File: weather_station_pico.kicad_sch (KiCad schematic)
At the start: 30 parts, among them J1 POWER, J2 WSPEED, J3 WDIR, J4 I2C, SW1 SW_Push, U1 LM7805_TO220, U2 E220-900T22D, U3 Pico, U4 74HC4051, U5 LM35-LP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

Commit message: ready for plot
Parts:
- gave numbers to parts that had none: 2
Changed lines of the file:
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@@
   (symbol (lib_id "Device:R") (at 148.59 144.78 0) (unit 1)
     (in_bom yes) (on_board yes) (fields_autoplaced)
-    (property "Reference" "R?" (id 0) (at 150.368 143.9453 0)
+    (property "Reference" "R6" (id 0) (at 150.368 143.9453 0)
       (effects (font (size 1.27 1.27)) (justify left))
     )
@@
   (symbol (lib_id "Device:R") (at 156.21 144.78 0) (unit 1)
     (in_bom yes) (on_board yes) (fields_autoplaced)
-    (property "Reference" "R?" (id 0) (at 157.988 143.9453 0)
+    (property "Reference" "R10" (id 0) (at 157.988 143.9453 0)
       (effects (font (size 1.27 1.27)) (justify left))
     )
@@
       (reference "R5") (unit 1) (value "18K") (footprint "Resistor_THT:R_Axial_DIN0207_L6.3mm_D2.5mm_P10.16mm_Horizontal")
     )
+    (path "/951b7f04-3bd9-48e0-a3b1-e47cb09aab6b"
+      (reference "R6") (unit 1) (value "10K") (footprint "Resistor_THT:R_Axial_DIN0207_L6.3mm_D2.5mm_P10.16mm_Horizontal")
+    )
     (path "/15b39b88-b949-4b93-a72b-6f012cecbbf8"
       (reference "R7") (unit 1) (value "10K") (footprint "Resistor_THT:R_Axial_DIN0207_L6.3mm_D2.5mm_P10.16mm_Horizontal")
@@
       (reference "R9") (unit 1) (value "10K") (footprint "Resistor_THT:R_Axial_DIN0207_L6.3mm_D2.5mm_P10.16mm_Horizontal")
     )
-    (path "/951b7f04-3bd9-48e0-a3b1-e47cb09aab6b"
-      (reference "R?") (unit 1) (value "10K") (footprint "Resistor_THT:R_Axial_DIN0207_L6.3mm_D2.5mm_P10.16mm_Horizontal")
-    )
     (path "/da2ad276-2e89-44d0-84db-4f891312c40c"
-      (reference "R?") (unit 1) (value "10K") (footprint "Resistor_THT:R_Axial_DIN0207_L6.3mm_D2.5mm_P10.16mm_Horizontal")
+      (reference "R10") (unit 1) (value "10K") (footprint "Resistor_THT:R_Axial_DIN0207_L6.3mm_D2.5mm_P10.16mm_Horizontal")
     )
     (path "/01ae44e4-73c7-4652-a3e0-80facd31ecc5"

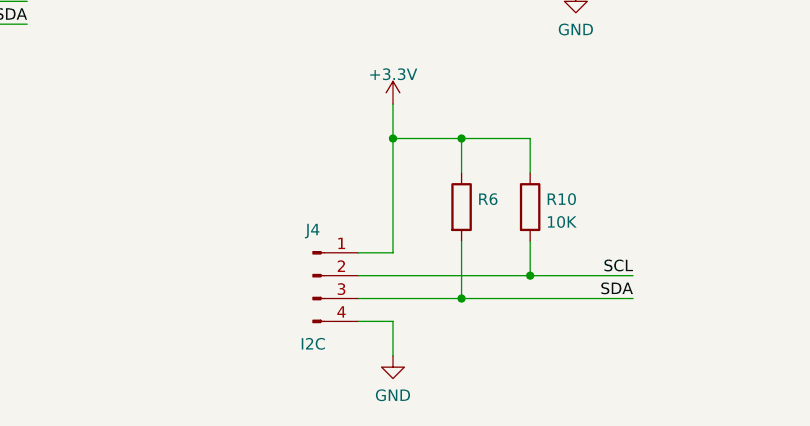
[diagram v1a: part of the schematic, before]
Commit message: add terminal, remove jst connector
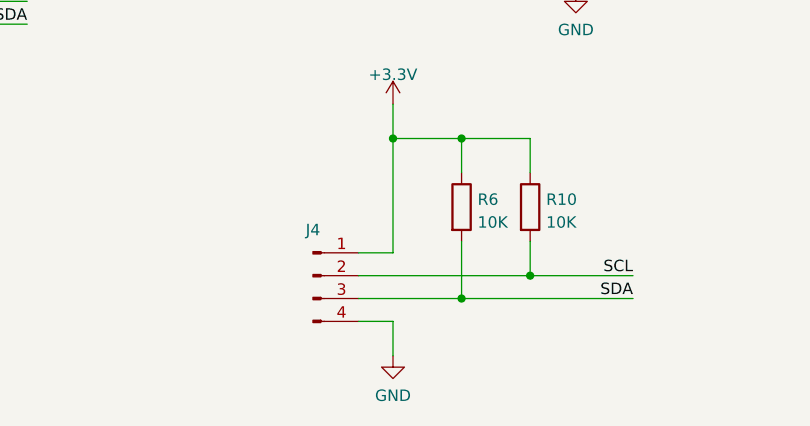
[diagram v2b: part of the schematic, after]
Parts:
- J1: footprint TerminalBlock_TE-Connectivity:TerminalBlock_TE_282834-2_1x02_P2.54mm_Horizontal -> TerminalBlock:TerminalBlock_bornier-2_P5.08mm
- J4: value I2C -> (none); footprint Connector_JST:JST_XH_B4B-XH-A_1x04_P2.50mm_Vertical -> (none)
- R6: value (none) -> 10K
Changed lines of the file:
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@@
     (in_bom yes) (on_board yes)
     (property "Reference" "J4" (id 0) (at 132.08 147.32 0))
-    (property "Value" "I2C" (id 1) (at 132.08 160.02 0))
-    (property "Footprint" "Connector_JST:JST_XH_B4B-XH-A_1x04_P2.50mm_Vertical" (id 2) (at 132.08 152.4 0)
+    (property "Value" "" (id 1) (at 132.08 160.02 0))
+    (property "Footprint" "" (id 2) (at 132.08 152.4 0)
       (effects (font (size 1.27 1.27)) hide)
     )
@@
     (property "Reference" "J1" (id 0) (at 41.91 26.7802 0))
     (property "Value" "POWER" (id 1) (at 41.91 29.3171 0))
-    (property "Footprint" "TerminalBlock_TE-Connectivity:TerminalBlock_TE_282834-2_1x02_P2.54mm_Horizontal" (id 2) (at 41.91 31.75 0)
+    (property "Footprint" "TerminalBlock:TerminalBlock_bornier-2_P5.08mm" (id 2) (at 41.91 31.75 0)
       (effects (font (size 1.27 1.27)) hide)
     )
@@
       (effects (font (size 1.27 1.27)) (justify left))
     )
-    (property "Value" "" (id 1) (at 150.368 146.4822 0)
+    (property "Value" "10K" (id 1) (at 150.368 146.4822 0)
       (effects (font (size 1.27 1.27)) (justify left))
     )
@@
     )
     (path "/950840dd-58ab-430d-9239-f8d51e62b21c"
-      (reference "J1") (unit 1) (value "POWER") (footprint "TerminalBlock_TE-Connectivity:TerminalBlock_TE_282834-2_1x02_P2.54mm_Horizontal")
+      (reference "J1") (unit 1) (value "POWER") (footprint "TerminalBlock:TerminalBlock_bornier-2_P5.08mm")
     )
     (path "/31f5e120-fc67-4891-91d3-9e217a46063f"
@@
     )
     (path "/52d6e53a-c8ef-4b23-a6a7-8729a222959a"
-      (reference "J4") (unit 1) (value "I2C") (footprint "Connector_JST:JST_XH_B4B-XH-A_1x04_P2.50mm_Vertical")
+      (reference "J4") (unit 1) (value "I2C") (footprint "TerminalBlock_TE-Connectivity:TerminalBlock_TE_282834-4_1x04_P2.54mm_Horizontal")
     )
     (path "/26932649-bf50-4889-b6d1-6949f1bf115e"

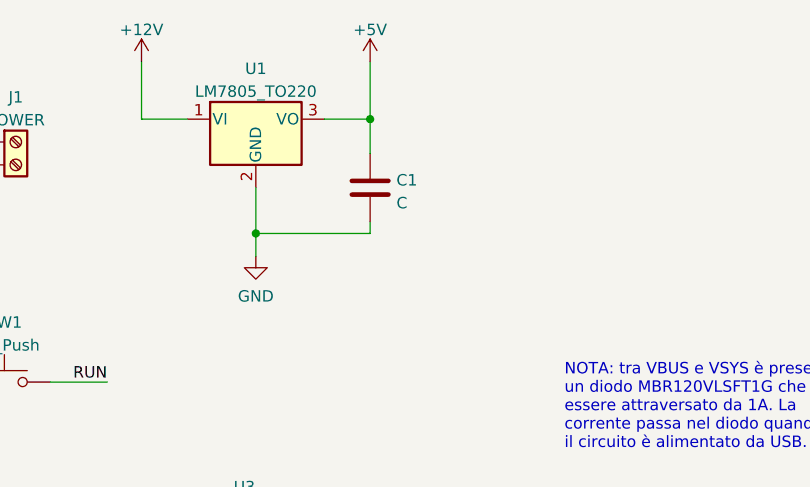
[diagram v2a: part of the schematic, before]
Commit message: move capacitor, more simple track
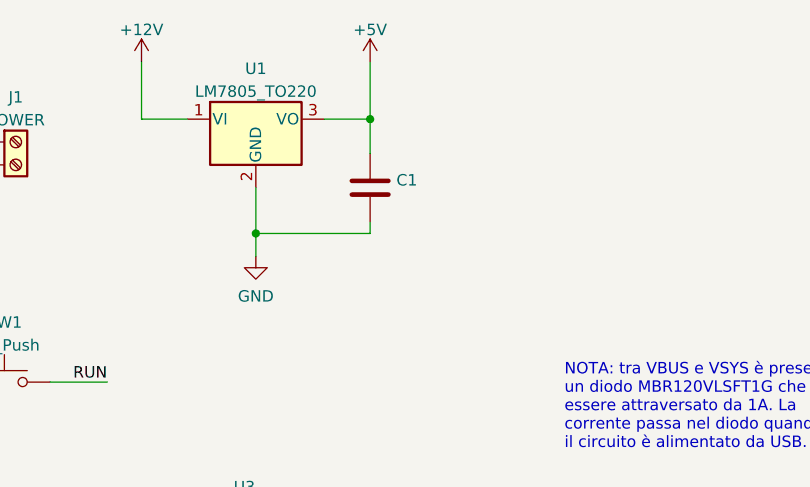
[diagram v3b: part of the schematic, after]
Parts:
- C1: value C -> (none)
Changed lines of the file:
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@@
       (effects (font (size 1.27 1.27)) (justify left))
     )
-    (property "Value" "C" (id 1) (at 84.201 38.5322 0)
+    (property "Value" "" (id 1) (at 84.201 38.5322 0)
       (effects (font (size 1.27 1.27)) (justify left))
     )
@@
     )
     (path "/eb529df0-006e-4c2f-99bd-b038e8ef398f"
-      (reference "C1") (unit 1) (value "C") (footprint "Capacitor_THT:C_Disc_D5.0mm_W2.5mm_P5.00mm")
+      (reference "C1") (unit 1) (value "0.1uF") (footprint "Capacitor_THT:C_Disc_D5.0mm_W2.5mm_P5.00mm")
     )
     (path "/6b3f8bcc-3de8-4f39-8ed0-7c34895de042"

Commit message: add millproject
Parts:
- removed TP1: TEMP_REF, TestPoint:TestPoint_Pad_D1.5mm, symbol Connector:TestPoint
- removed TP2: GND, TestPoint:TestPoint_Pad_D1.5mm, symbol Connector:TestPoint
- removed TP3: TEMP_OUT, TestPoint:TestPoint_Pad_D1.5mm, symbol Connector:TestPoint
- removed TP4: MUX_ADC, TestPoint:TestPoint_Pad_D1.5mm, symbol Connector:TestPoint
- C1: value (none) -> 0.1uF
- J4: value (none) -> I2C; footprint (none) -> TerminalBlock_TE-Connectivity:TerminalBlock_TE_282834-4_1x04_P2.54mm_Horizontal
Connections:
- net GND: no longer U3.42 (GND)
- no-connect marks 21 -> 22
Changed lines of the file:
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@@
   (junction (at 140.97 137.16) (diameter 0) (color 0 0 0 0)
   )
-  (junction (at 146.05 91.44) (diameter 0) (color 0 0 0 0)
-  )
   (junction (at 153.67 26.67) (diameter 0) (color 0 0 0 0)
   )
@@
   (junction (at 34.29 31.75) (diameter 0) (color 0 0 0 0)
   )
-  (junction (at 180.34 99.06) (diameter 0) (color 0 0 0 0)
-  )
   (junction (at 260.35 76.2) (diameter 0) (color 0 0 0 0)
-  )
-  (junction (at 182.88 91.44) (diameter 0) (color 0 0 0 0)
   )
   (junction (at 34.29 34.29) (diameter 0) (color 0 0 0 0)
@@
   (no_connect (at 171.45 104.14))
   (no_connect (at 171.45 101.6))
+  (no_connect (at 67.31 129.54))
   (no_connect (at 49.53 83.82))
   (no_connect (at 49.53 76.2))
@@
     (stroke (width 0) (type default) (color 0 0 0 0))
   )
-  (wire (pts (xy 180.34 99.06) (xy 203.2 99.06))
+  (wire (pts (xy 171.45 99.06) (xy 203.2 99.06))
     (stroke (width 0) (type default) (color 0 0 0 0))
   )
@@
     (stroke (width 0) (type default) (color 0 0 0 0))
   )
-  (wire (pts (xy 146.05 81.28) (xy 146.05 91.44))
-    (stroke (width 0) (type default) (color 0 0 0 0))
-  )
   (wire (pts (xy 68.58 36.83) (xy 68.58 41.91))
     (stroke (width 0) (type default) (color 0 0 0 0))
@@
     (stroke (width 0) (type default) (color 0 0 0 0))
   )
-  (wire (pts (xy 151.13 116.84) (xy 161.29 116.84))
-    (stroke (width 0) (type default) (color 0 0 0 0))
-  )
   (wire (pts (xy 153.67 26.67) (xy 168.91 26.67))
     (stroke (width 0) (type default) (color 0 0 0 0))
@@
     (stroke (width 0) (type default) (color 0 0 0 0))
   )
-  (wire (pts (xy 171.45 99.06) (xy 180.34 99.06))
-    (stroke (width 0) (type default) (color 0 0 0 0))
-  )
   (wire (pts (xy 148.59 137.16) (xy 156.21 137.16))
     (stroke (width 0) (type default) (color 0 0 0 0))
@@
     (stroke (width 0) (type default) (color 0 0 0 0))
   )
-  (wire (pts (xy 146.05 91.44) (xy 153.67 91.44))
-    (stroke (width 0) (type default) (color 0 0 0 0))
-  )
-  (wire (pts (xy 133.35 91.44) (xy 146.05 91.44))
+  (wire (pts (xy 133.35 91.44) (xy 153.67 91.44))
     (stroke (width 0) (type default) (color 0 0 0 0))
   )
@@
     (stroke (width 0) (type default) (color 0 0 0 0))
   )
-  (wire (pts (xy 182.88 91.44) (xy 203.2 91.44))
+  (wire (pts (xy 171.45 91.44) (xy 203.2 91.44))
     (stroke (width 0) (type default) (color 0 0 0 0))
   )
@@
     (stroke (width 0) (type default) (color 0 0 0 0))
   )
-  (wire (pts (xy 180.34 78.74) (xy 180.34 99.06))
-    (stroke (width 0) (type default) (color 0 0 0 0))
-  )
   (wire (pts (xy 260.35 25.4) (xy 260.35 27.94))
     (stroke (width 0) (type default) (color 0 0 0 0))
@@
     (stroke (width 0) (type default) (color 0 0 0 0))
   )
-  (wire (pts (xy 171.45 91.44) (xy 182.88 91.44))
-    (stroke (width 0) (type default) (color 0 0 0 0))
-  )
   (wire (pts (xy 137.16 157.48) (xy 140.97 157.48))
     (stroke (width 0) (type default) (color 0 0 0 0))
@@
     (stroke (width 0) (type default) (color 0 0 0 0))
   )
-  (wire (pts (xy 182.88 83.82) (xy 182.88 91.44))
-    (stroke (width 0) (type default) (color 0 0 0 0))
-  )
   (wire (pts (xy 168.91 26.67) (xy 168.91 34.29))
     (stroke (width 0) (type default) (color 0 0 0 0))
@@
   )
   (wire (pts (xy 180.34 26.67) (xy 180.34 29.21))
-    (stroke (width 0) (type default) (color 0 0 0 0))
-  )
-  (wire (pts (xy 67.31 129.54) (xy 67.31 135.89))
     (stroke (width 0) (type default) (color 0 0 0 0))
   )
@@
     (pin "1")
   )
-  (symbol (lib_id "Connector:TestPoint") (at 151.13 116.84 90) (unit 1)
-    (in_bom yes) (on_board yes) (fields_autoplaced)
-    (property "Reference" "TP2" (id 0) (at 147.828 112.5052 90))
-    (property "Value" "GND" (id 1) (at 147.828 115.0421 90))
-    (property "Footprint" "TestPoint:TestPoint_Pad_D1.5mm" (id 2) (at 151.13 111.76 0)
-      (effects (font (size 1.27 1.27)) hide)
-    )
-    (property "Datasheet" "~" (id 3) (at 151.13 111.76 0)
-      (effects (font (size 1.27 1.27)) hide)
-    )
-    (pin "1")
-  )
-  (symbol (lib_id "Connector:TestPoint") (at 146.05 81.28 0) (mirror y) (unit 1)
-    (in_bom yes) (on_board yes)
-    (property "Reference" "TP4" (id 0) (at 144.78 76.2 0)
-      (effects (font (size 1.27 1.27)) (justify left))
-    )
-    (property "Value" "MUX_ADC" (id 1) (at 144.78 78.74 0)
-      (effects (font (size 1.27 1.27)) (justify left))
-    )
-    (property "Footprint" "TestPoint:TestPoint_Pad_D1.5mm" (id 2) (at 140.97 81.28 0)
-      (effects (font (size 1.27 1.27)) hide)
-    )
-    (property "Datasheet" "~" (id 3) (at 140.97 81.28 0)
-      (effects (font (size 1.27 1.27)) hide)
-    )
-    (pin "1")
-  )
   (symbol (lib_id "Sensor_Temperature:LM35-LP") (at 228.6 124.46 0) (unit 1)
     (in_bom yes) (on_board yes) (fields_autoplaced)
@@
     (pin "1")
   )
-  (symbol (lib_id "Connector:TestPoint") (at 182.88 83.82 0) (unit 1)
-    (in_bom yes) (on_board yes) (fields_autoplaced)
-    (property "Reference" "TP3" (id 0) (at 184.277 79.6833 0)
-      (effects (font (size 1.27 1.27)) (justify left))
-    )
-    (property "Value" "TEMP_OUT" (id 1) (at 184.277 82.2202 0)
-      (effects (font (size 1.27 1.27)) (justify left))
-    )
-    (property "Footprint" "TestPoint:TestPoint_Pad_D1.5mm" (id 2) (at 187.96 83.82 0)
-      (effects (font (size 1.27 1.27)) hide)
-    )
-    (property "Datasheet" "~" (id 3) (at 187.96 83.82 0)
-      (effects (font (size 1.27 1.27)) hide)
-    )
-    (pin "1")
-  )
   (symbol (lib_id "Connector:Conn_01x04_Male") (at 132.08 152.4 0) (unit 1)
     (in_bom yes) (on_board yes)
     (property "Reference" "J4" (id 0) (at 132.08 147.32 0))
-    (property "Value" "" (id 1) (at 132.08 160.02 0))
-    (property "Footprint" "" (id 2) (at 132.08 152.4 0)
+    (property "Value" "I2C" (id 1) (at 132.08 160.02 0))
+    (property "Footprint" "TerminalBlock_TE-Connectivity:TerminalBlock_TE_282834-4_1x04_P2.54mm_Horizontal" (id 2) (at 132.08 152.4 0)
       (effects (font (size 1.27 1.27)) hide)
     )
@@
     )
     (property "Datasheet" "" (id 3) (at 161.29 120.65 0)
-      (effects (font (size 1.27 1.27)) hide)
-    )
-    (pin "1")
-  )
-  (symbol (lib_id "power:GND") (at 67.31 135.89 0) (unit 1)
-    (in_bom yes) (on_board yes) (fields_autoplaced)
-    (property "Reference" "#PWR0103" (id 0) (at 67.31 142.24 0)
-      (effects (font (size 1.27 1.27)) hide)
-    )
-    (property "Value" "GND" (id 1) (at 67.31 140.3334 0))
-    (property "Footprint" "" (id 2) (at 67.31 135.89 0)
-      (effects (font (size 1.27 1.27)) hide)
-    )
-    (property "Datasheet" "" (id 3) (at 67.31 135.89 0)
-      (effects (font (size 1.27 1.27)) hide)
-    )
-    (pin "1")
-  )
-  (symbol (lib_id "Connector:TestPoint") (at 180.34 78.74 0) (unit 1)
-    (in_bom yes) (on_board yes) (fields_autoplaced)
-    (property "Reference" "TP1" (id 0) (at 181.737 74.6033 0)
-      (effects (font (size 1.27 1.27)) (justify left))
-    )
-    (property "Value" "TEMP_REF" (id 1) (at 181.737 77.1402 0)
-      (effects (font (size 1.27 1.27)) (justify left))
-    )
-    (property "Footprint" "TestPoint:TestPoint_Pad_D1.5mm" (id 2) (at 185.42 78.74 0)
-      (effects (font (size 1.27 1.27)) hide)
-    )
-    (property "Datasheet" "~" (id 3) (at 185.42 78.74 0)
       (effects (font (size 1.27 1.27)) hide)
     )
@@
       (effects (font (size 1.27 1.27)) (justify left))
     )
-    (property "Value" "" (id 1) (at 84.201 38.5322 0)
+    (property "Value" "0.1uF" (id 1) (at 84.201 38.5322 0)
       (effects (font (size 1.27 1.27)) (justify left))
     )
@@
       (reference "#PWR0102") (unit 1) (value "GND") (footprint "")
     )
-    (path "/86292fc3-6883-4ad4-abac-0fcfd4ef342c"
-      (reference "#PWR0103") (unit 1) (value "GND") (footprint "")
-    )
     (path "/cde70252-7615-43f7-b7b6-116ad0ec304c"
       (reference "#PWR0104") (unit 1) (value "GND") (footprint "")
@@
       (reference "SW1") (unit 1) (value "SW_Push") (footprint "Button_Switch_THT:SW_PUSH_6mm_H5mm")
     )
-    (path "/8a466b04-98ce-43f9-8458-1c0ae7ad8c6e"
-      (reference "TP1") (unit 1) (value "TEMP_REF") (footprint "TestPoint:TestPoint_Pad_D1.5mm")
-    )
-    (path "/3b00fbcb-c057-4240-b7a6-4dd3be7f0496"
-      (reference "TP2") (unit 1) (value "GND") (footprint "TestPoint:TestPoint_Pad_D1.5mm")
-    )
-    (path "/50fbf6cc-85f4-46c7-991c-01ed4ce42876"
-      (reference "TP3") (unit 1) (value "TEMP_OUT") (footprint "TestPoint:TestPoint_Pad_D1.5mm")
-    )
-    (path "/3ca073c5-0c4b-4dcb-b598-99ba8ef38fa2"
-      (reference "TP4") (unit 1) (value "MUX_ADC") (footprint "TestPoint:TestPoint_Pad_D1.5mm")
-    )
     (path "/e36b28a4-7427-4708-a63e-3fe312e8d49f"
